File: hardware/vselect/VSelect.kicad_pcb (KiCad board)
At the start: 2 copper layers, 15.4 x 10 mm, 10 parts, among them U1 TPS2113PW

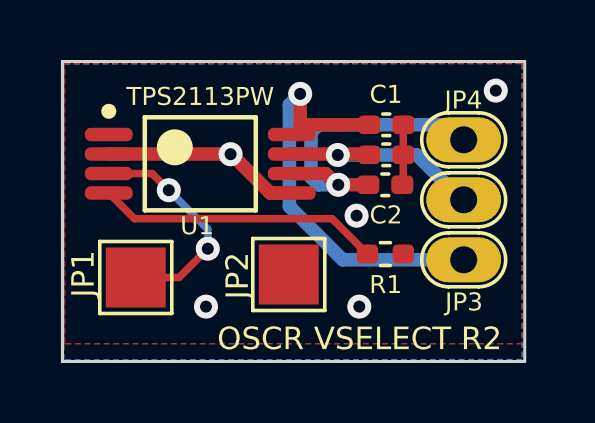
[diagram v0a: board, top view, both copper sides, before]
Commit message: VSELECT Module Rev 3
Refreshed things a bit to improve clarity, make installation easier, and to reduce costs when manufacturing in bulk. There is no reason to upgrade already installed modules to this revision.

* Changed the module to be installed on the back of the PCB again as it is much easier to install that way.
* Added pad for the STAT pin. There's no real use for this at the moment.
* Changed the layout slightly to allow room for all of the capacitors' legends. This should make things more clear when assembling a module by hand.
* Changed the legends for the jumper pads to use the net name instead of the designator. This should make things easier during installation.
* Added legends to specify 3.3V/5V for the pads that connect to the power switch footprint. Hopefully, this helps keep people from installing the module incorrectly.
* Updated the TPS2113 footprint to the new one that allows using either the TSSOP or SON package. This should give more flexibility regarding part availability.
* Changed part numbers to more readily available parts. This should reduce the cost of machine assembly.
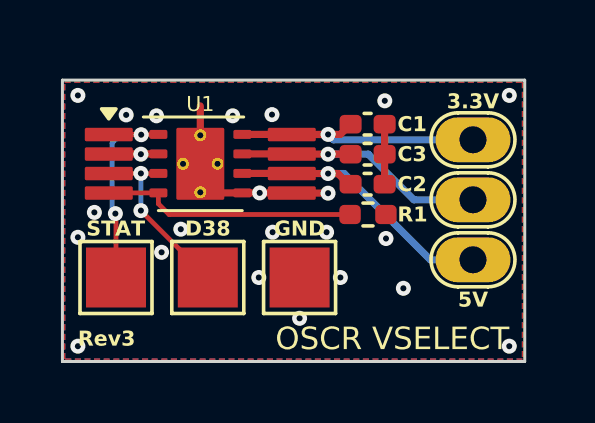
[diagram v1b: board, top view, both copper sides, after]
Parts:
- added JP6: VS_STAT, TestPoint:TestPoint_Pad_2.0x2.0mm, F.Cu at (28.7, 24.6)
- C1, C2: value 0.1 uF -> 0.1u
- C3: value 10 uF -> 10u
- JP3, JP4, JP5: footprint Personal:Vpower-Switch-Pad -> !OSCRMisc:Header - VSELECT - Switch Pad
- R1: value 550 -> 560R
- U1: value TPS2113PW -> TPS2113; footprint Personal:Texas_Instruments-TPS2113PW-Level_A -> !OSCRMisc:IC - VSELECT - TPS2113
- moved JP4 5.11 mm to (40.6, 24.0), turned to 180 degrees
- moved JP3 2.92 mm to (40.6, 20.0), turned to 180 degrees
- moved JP1 2.40 mm to (31.8, 24.6)
- moved R1 1.44 mm to (37.1, 22.5)
- moved JP5 1.14 mm to (40.6, 22.0), turned to 180 degrees
- moved C1 0.62 mm to (37.1, 19.5)
- moved C3 0.62 mm to (37.1, 20.5)
- moved C2 0.59 mm to (37.1, 21.5)
- moved JP2 0.37 mm to (34.9, 24.6)
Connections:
- net Net-(R1-Pad2) renamed /ILIM
- U1 pad 1: unconnected-(U1-Pad1) -> VS_STAT
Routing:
- net VS_STAT: track 0.00 -> 7.35 mm, vias 0 -> 2
- net +3.3V: track 13.8 -> 10.6 mm
- net VCC: track 7.40 -> 9.39 mm
- net VSELECT: track 7.52 -> 6.05 mm
- net GND: track 8.65 -> 9.63 mm, vias 5 -> 23
- net /ILIM: track 9.47 -> 8.56 mm
- net +5V: track 10.6 -> 9.78 mm
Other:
- board size 15.4 x 10 mm -> 15.4 x 9.4 mm
- board text added: "${CURRENT_DATE}"
- board text added: "D38"
- board text added: "GND"
- board text added: "JLCJLCJLCJLC"
- board text added: "OSCR VSELECT"
- board text added: "Rev${REVISION}"
- board text added: "STAT"
- board text removed: "OSCR VSELECT R2"

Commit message: Fix/cleanup the VSELECT Module project files
* Fixed the field name for the LCSC part number so the BOM exports with the part numbers.
* Removed the test points from the schematic as they are no longer needed.
* Added notes for setting the ILIM resistor to the schematic.
* Added an image of the PCB and PDF of the schematic.

Note: The PCB itself didn't change, so it is still Rev 3.
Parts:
- U1: value TPS2113 -> TPS211x
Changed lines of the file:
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@@
-			)
-		)
-		(property "JLCPCB" "C1525"
-			(at 75.5 38.98 0)
-			(layer "F.Fab")
-			(hide yes)
-			(effects
-				(font
-					(size 1 1)
-					(thickness 0.15)
-				)
 			)
 		)
 		(property "Part" "CL05B104KO5NNNC"
+			(at 0 0 180)
+			(unlocked yes)
+			(layer "F.Fab")
+			(hide yes)
+			(effects
+				(font
+					(size 1 1)
+					(thickness 0.15)
+				)
+			)
+		)
+		(property "LCSC" "C1525"
 			(at 0 0 180)
 			(unlocked yes)
@@
 			)
 		)
-		(property "Value" "TPS2113"
+		(property "Value" "TPS211x"
 			(at 0 1.6 0)
 			(layer "F.Fab")
@@
 			)
 		)
-		(property "JLCPCB" ""
+		(property "Note" "You can substitute a TPS2112, just be sure to update the value of R1."
 			(at 0 0 0)
 			(unlocked yes)
@@
 			)
 		)
-		(property "JLCPCB" "C1525"
-			(at 0 0 0)
-			(layer "F.Fab")
-			(hide yes)
-			(effects
-				(font
-					(size 1 1)
-					(thickness 0.15)
-				)
-			)
-		)
 		(property "Part" "CL05B104KO5NNNC"
+			(at 0 0 0)
+			(unlocked yes)
+			(layer "F.Fab")
+			(hide yes)
+			(effects
+				(font
+					(size 1 1)
+					(thickness 0.15)
+				)
+			)
+		)
+		(property "LCSC" "C1525"
 			(at 0 0 0)
 			(unlocked yes)
@@
 			)
 		)
-		(property "JLCPCB" "C15525"
-			(at 0 0 0)
-			(layer "F.Fab")
-			(hide yes)
-			(effects
-				(font
-					(size 1 1)
-					(thickness 0.15)
-				)
-			)
-		)
 		(property "Part" "CL05A106MQ5NUNC"
+			(at 0 0 0)
+			(unlocked yes)
+			(layer "F.Fab")
+			(hide yes)
+			(effects
+				(font
+					(size 1 1)
+					(thickness 0.15)
+				)
+			)
+		)
+		(property "LCSC" "C15525"
 			(at 0 0 0)
 			(unlocked yes)
@@
 			)
 		)
-		(property "JLCPCB" "C25123"
-			(at 75.44 47.6 0)
-			(layer "F.Fab")
-			(hide yes)
-			(effects
-				(font
-					(size 1 1)
-					(thickness 0.15)
-				)
-			)
-		)
 		(property "Alt Parts" "1.12A/560R (C137858); 0.98A/510R (C25123)"
 			(at 0 0 180)
@@
 			(at 0 0 180)
 			(unlocked yes)
+			(layer "F.Fab")
+			(hide yes)
+			(effects
+				(font
+					(size 1 1)
+					(thickness 0.15)
+				)
+			)
+		)
+		(property "LCSC" "C25123"
+			(at 0 0 180)
+			(unlocked yes)
+			(layer "F.Fab")
+			(hide yes)
+			(effects
+				(font
+					(size 1 1)
+					(thickness 0.15)
+				)
+			)
+		)
+		(property "Part" "0402WGF5100TCE"
+			(at 0 0 180)
+			(unlocked yes)
